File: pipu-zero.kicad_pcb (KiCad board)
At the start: 4 copper layers, 80 x 50.5 mm, 82 parts, among them IC1 BQ25176JDSGR, J1 USB_C_Receptacle_USB2.0_14P, J2 Conn_01x08, J3 Micro_SD_Card_Det1, Q1 NMOS, Q2 NMOS, Q3 NMOS, Q4 NMOS, SW1 SW_Push, SW2 SW_Push, U1 BQ297xy, U2 MCP1640Bx-xCHY, U3 MCP1727-0802xSN, U4 ESP32-S3-WROOM-1, U5 CC1101, U6 DM-OLED096-636, U7 TSOP348xx, Y2 Crystal_GND23

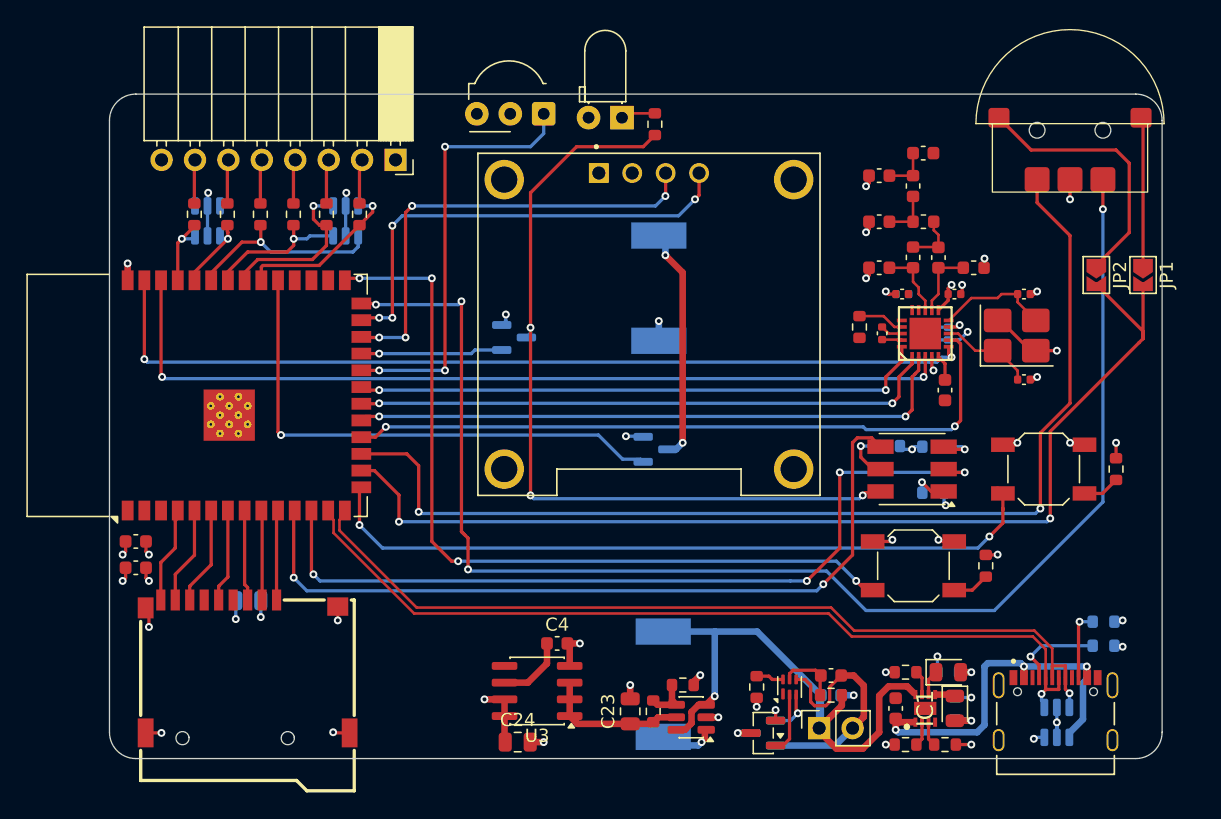
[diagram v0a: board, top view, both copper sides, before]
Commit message: add antenna connector
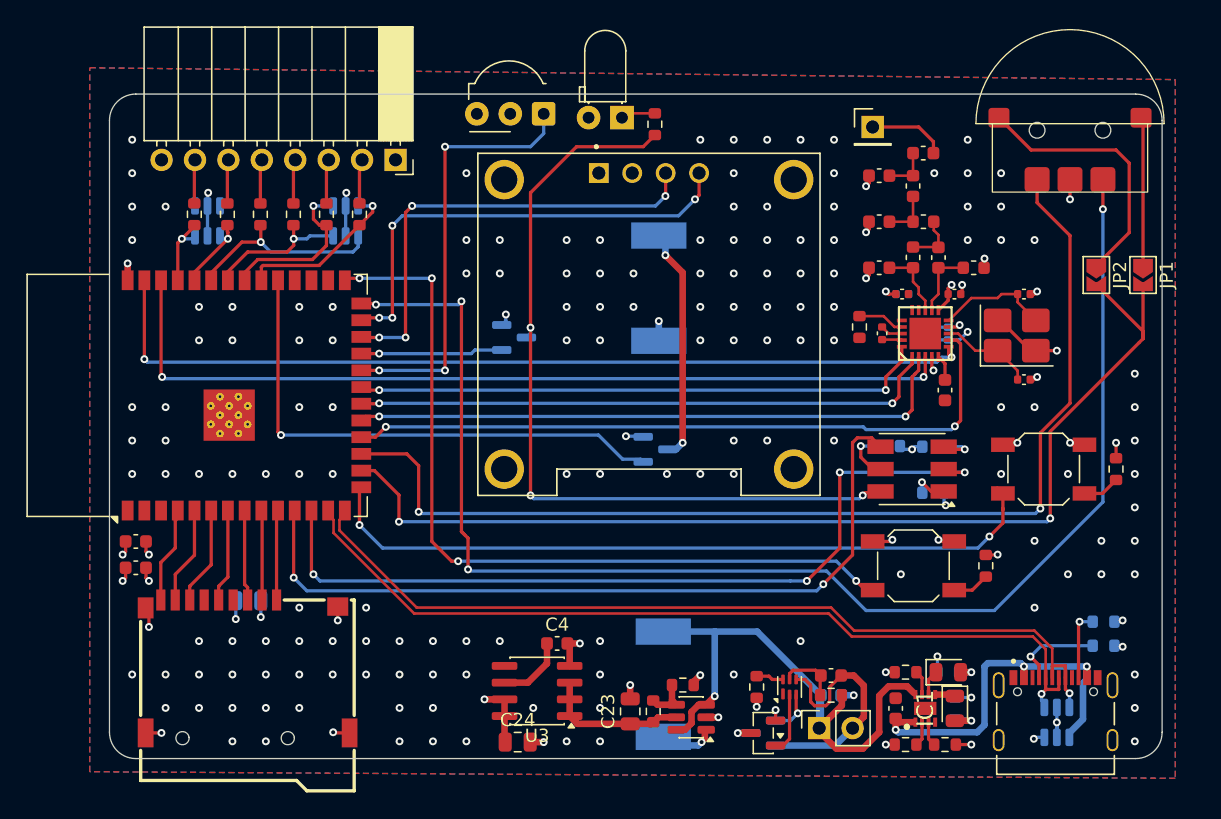
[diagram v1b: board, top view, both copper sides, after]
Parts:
- added AE1: Antenna, Connector_PinHeader_2.54mm:PinHeader_1x01_P2.54mm_Vertical, F.Cu at (171.5, 65.0)
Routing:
- net Net-(AE1-A): track 0.00 -> 5.95 mm
- net GND: vias 41 -> 192
- added copper zone on In2.Cu, net +3V3
- added copper zone on B.Cu, net GND
- added copper zone on F.Cu, net GND
- added copper zone on In1.Cu, net GND
- removed copper zone on In1.Cu, net +3V3
- removed copper zone on In2.Cu, net GND

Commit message: LUIGI
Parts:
- removed AE1: Antenna, Connector_PinHeader_2.54mm:PinHeader_1x01_P2.54mm_Vertical
- C10, C11, C12, C13, C5, C7, C8, C9: value C -> 100n
- C14, C15: value C_Small -> 14p
- C16, C17: value C -> 3.9p
- C18: value C -> 8.2p
- C19: value C -> 5.6p
- C20: value C -> 220p
- C23, C24, C25, C6: value C -> 10u
- R1, R2: value R_Small -> 5.1k
- R10: value R_Small -> 562
- R11: value R -> 100R
- R12: value R -> 56k
- R13: value R_Small -> 100
- R14, R15, R16, R17, R18: value R_Small -> 100R
- R19, R21: value R -> 10k
- R22: value R -> 20k
- R23, R24, R25: value R -> 100
- R9: value R_Small -> 976
- Y2: value Crystal_GND23 -> X322526MMB4SI
- moved C6 1.00 mm to (115.5, 97.5)
- moved C5 0.50 mm to (115.5, 96.0)
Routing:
- net Net-(AE1-A): track 5.95 -> 0.00 mm
- net +3V3: track 26.0 -> 29.7 mm, vias 15 -> 14
- net GND: track 57.3 -> 59.8 mm, vias 192 -> 40
- added copper zone on In1.Cu, net +3V3
- added copper zone on In2.Cu, net GND
- removed copper zone on In2.Cu, net +3V3
- removed copper zone on B.Cu, net GND
- removed copper zone on F.Cu, net GND
- removed copper zone on In1.Cu, net GND
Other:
- board text added: "<- LUIGI"

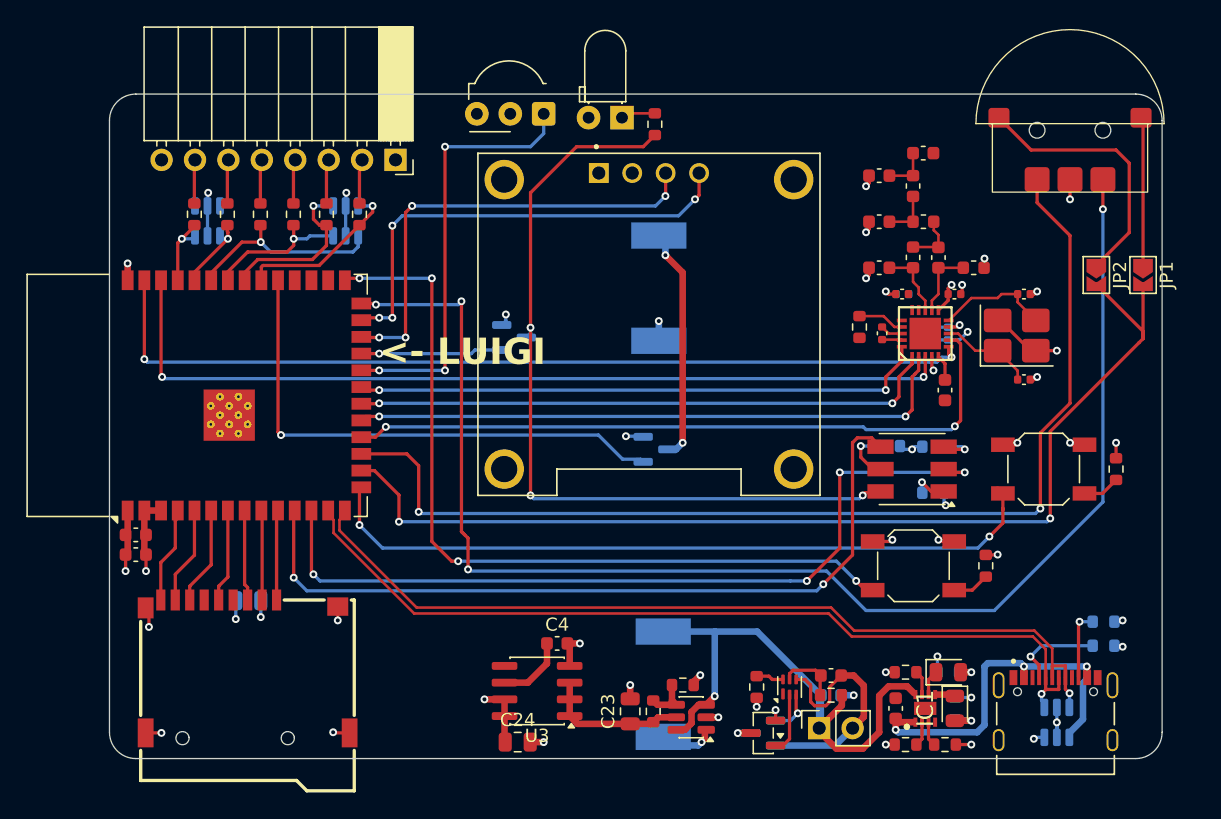
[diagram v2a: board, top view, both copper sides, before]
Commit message: add silkscreen
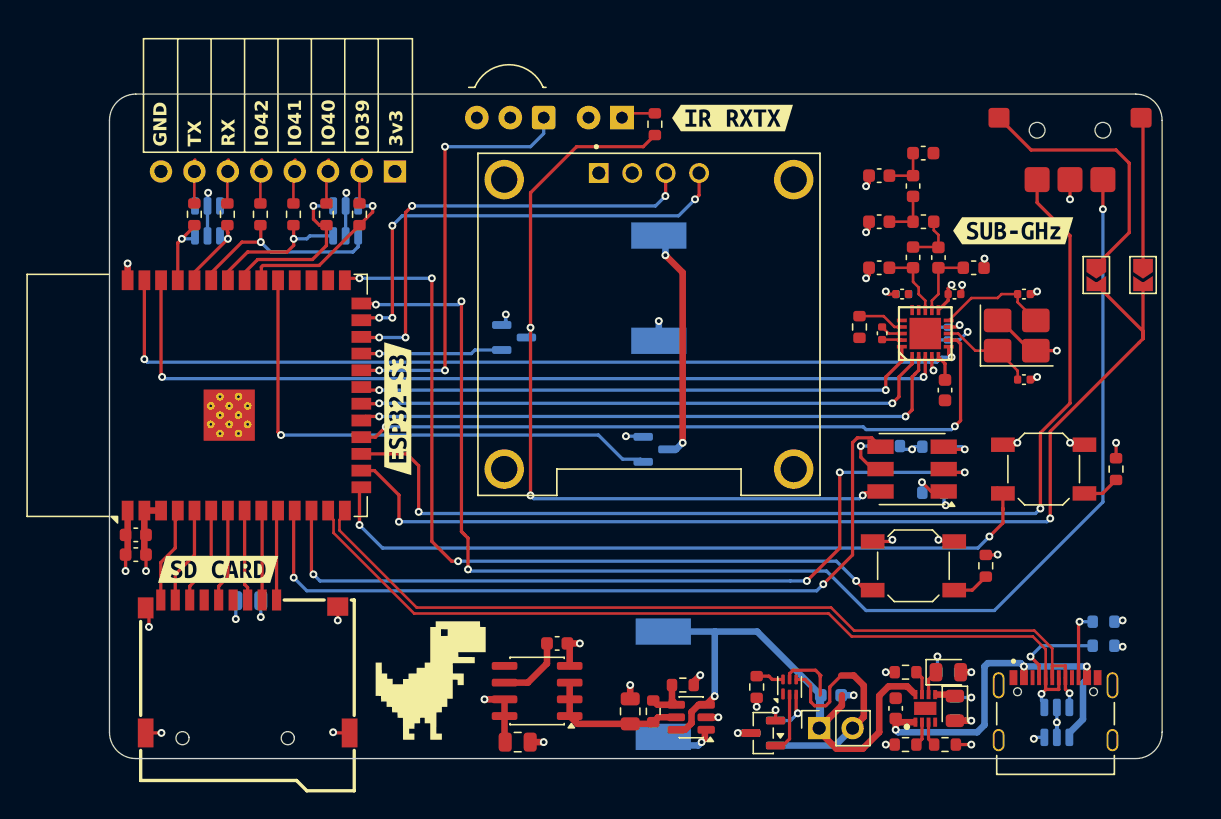
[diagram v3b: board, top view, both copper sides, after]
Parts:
- removed C2: 100n, Capacitor_SMD:C_0603_1608Metric
- removed R3: 330, Resistor_SMD:R_0603_1608Metric
- added G***: LOGO, LOGO, F.Cu at (137.9, 107.1)
- added kibuzzard-6926C46D: G***, kibuzzard-6926C46D, F.Cu at (121.8, 98.6)
- added kibuzzard-6926C4AC: G***, kibuzzard-6926C4AC, F.Cu at (160.8, 64.3)
- added kibuzzard-6926C4FB: G***, kibuzzard-6926C4FB, F.Cu at (182.2, 72.9)
- added kibuzzard-6926C534: G***, kibuzzard-6926C534, F.Cu at (135.4, 86.4)
- moved J2 0.88 mm to (135.2, 68.4)
- moved U7 0.29 mm to (146.5, 64.3)
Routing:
- net /I-O/TXD0_EXT: track 3.33 -> 2.51 mm
- net /I-O/RXD0_EXT: track 3.35 -> 2.56 mm
- net /I-O/IO42_EXT: track 3.36 -> 2.61 mm
- net /I-O/IO41_EXT: track 3.37 -> 2.67 mm
- net /I-O/IO40_EXT: track 3.38 -> 2.72 mm
- net /I-O/IO39_EXT: track 3.40 -> 2.78 mm
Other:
- board text added: "3v3"
- board text added: "GND"
- board text added: "IO39"
- board text added: "IO40"
- board text added: "IO41"
- board text added: "IO42"
- board text added: "LUIGI"
- board text added: "RX"
- board text added: "TX"
- board text removed: "<- LUIGI"

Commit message: Add top and bottom ground plane
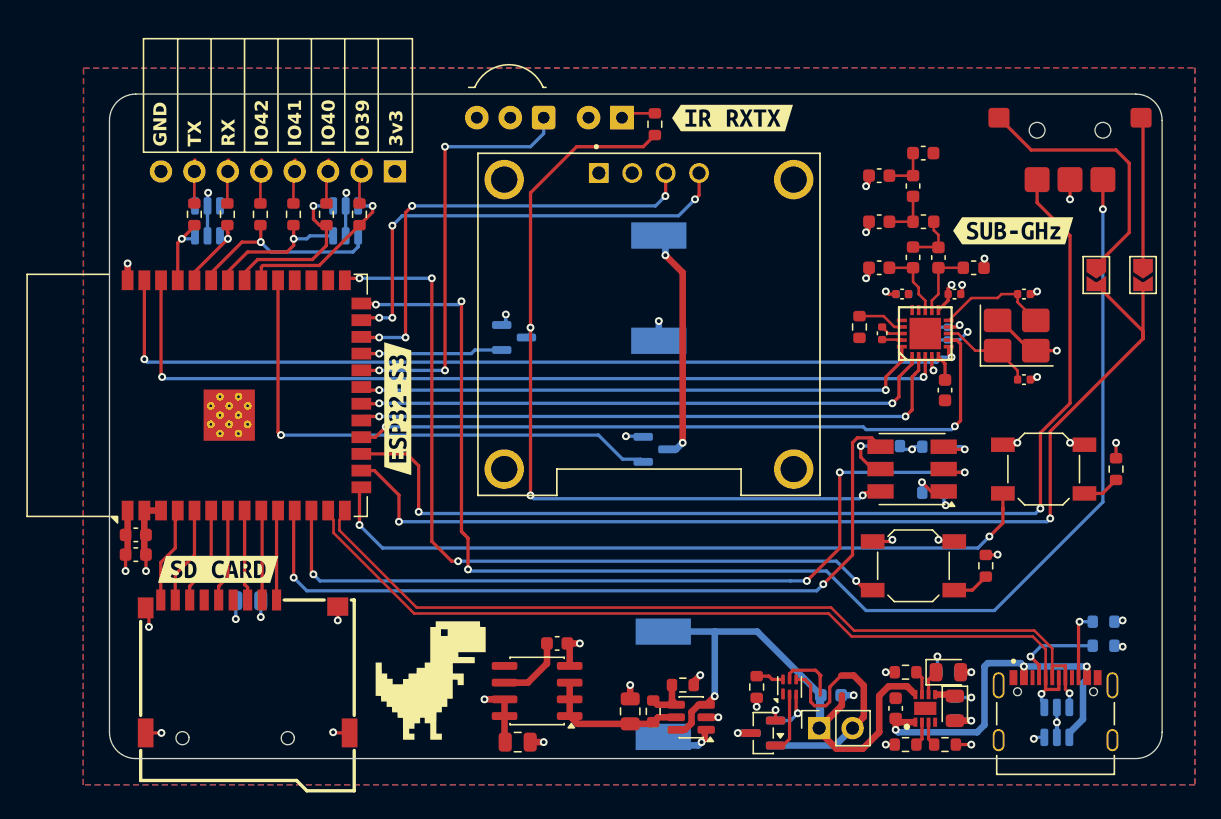
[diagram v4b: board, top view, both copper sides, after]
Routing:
- added copper zone on B.Cu, net GND
- added copper zone on F.Cu, net GND
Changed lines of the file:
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@@
 				(font
 					(size 0.001 0.001)
+					(thickness 0.15)
 				)
 			)
@@
 				(font
 					(size 0.001 0.001)
+					(thickness 0.15)
 				)
 			)
@@
 				(font
 					(size 0.001 0.001)
+					(thickness 0.15)
 				)
 			)
@@
 				(font
 					(size 0.001 0.001)
+					(thickness 0.15)
 				)
 			)
@@
 				(font
 					(size 0.001 0.001)
+					(thickness 0.15)
 				)
 			)
@@
 				(font
 					(size 0.001 0.001)
+					(thickness 0.15)
 				)
 			)
@@
 				(font
 					(size 0.001 0.001)
+					(thickness 0.15)
 				)
 			)
@@
 				(font
 					(size 0.001 0.001)
+					(thickness 0.15)
 				)
 			)
@@
 	)
 	(zone
-		(net 8)
-		(net_name "+3V3")
-		(layer "In1.Cu")
+		(net 3)
+		(net_name "GND")
+		(layers "F.Cu" "B.Cu" "In2.Cu")
 		(hatch edge 0.5)
+		(priority 1)
 		(connect_pads
 			(clearance 0.5)
@@
 		(polygon
 			(pts
-				(xy 111.527834 60.527834) (xy 111.5 115) (xy 196 115) (xy 196 60.5)
+				(xy 111.527834 60.527834) (xy 196 60.5) (xy 196 115) (xy 111.5 115)
 			)
 		)
 	)
 	(zone
-		(net 3)
-		(net_name "GND")
-		(layer "In2.Cu")
+		(net 8)
+		(net_name "+3V3")
+		(layer "In1.Cu")
 		(hatch edge 0.5)
-		(priority 1)
 		(connect_pads
 			(clearance 0.5)
@@
 		(polygon
 			(pts
-				(xy 111.527834 60.527834) (xy 196 60.5) (xy 196 115) (xy 111.5 115)
+				(xy 111.527834 60.527834) (xy 111.5 115) (xy 196 115) (xy 196 60.5)
 			)
 		)

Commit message: fix drc
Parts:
- added C2: 100n, Capacitor_SMD:C_0603_1608Metric, F.Cu at (168.7, 107.4)
- added R3: 330, Resistor_SMD:R_0603_1608Metric, F.Cu at (167.1, 107.4)
- moved R21 0.52 mm to (179.6, 98.3)
- moved R22 0.52 mm to (189.5, 90.9)
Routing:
- net GND: track 59.8 -> 73.6 mm
- net +3V3: track 29.7 -> 36.2 mm, vias 14 -> 16
- net Net-(BT1--): track 18.6 -> 12.9 mm
- net /Power Manager/BAT+: track 43.4 -> 42.7 mm

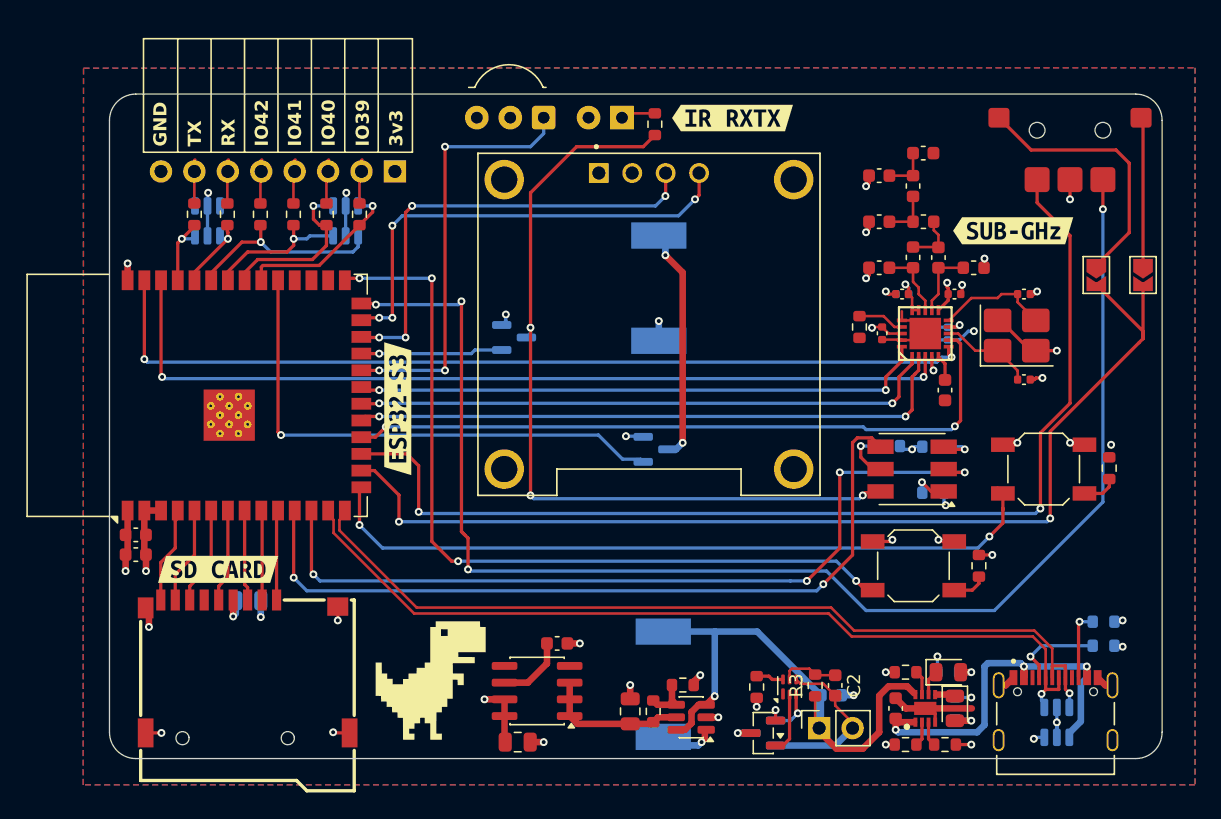
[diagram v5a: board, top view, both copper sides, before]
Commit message: add vias
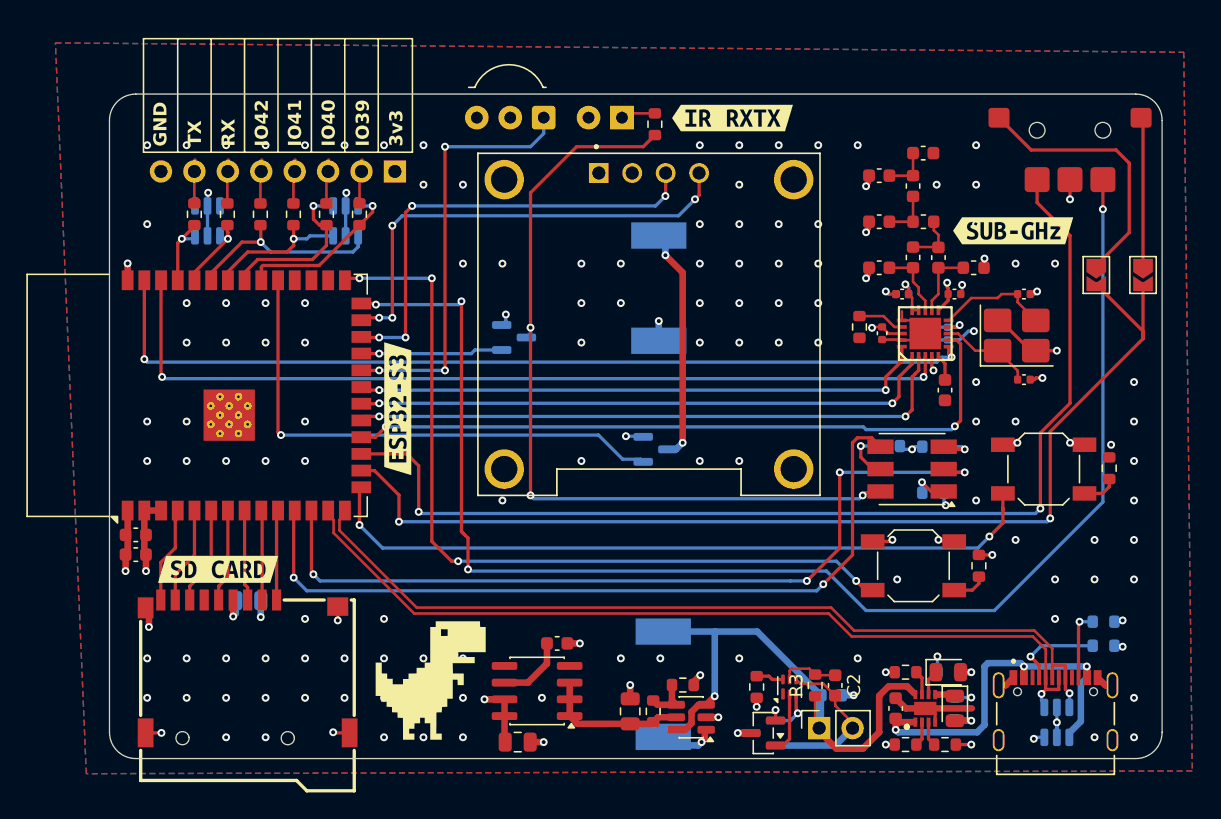
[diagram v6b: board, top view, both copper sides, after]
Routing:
- net GND: vias 40 -> 156
